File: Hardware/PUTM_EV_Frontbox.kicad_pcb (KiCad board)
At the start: 4 copper layers, 97 x 73 mm, 188 parts, among them IC1 TPS54202HDDCR, J1 XIAO ESP32S3 Sense, J2 Conn_02x16_Counter_Clockwise, J3 FTSH-107-01-L-D-K, Q1 SI2347DS-T1-GE3, U1 TLV743P, U10 MCP6N11-001E/SN, U11 MCP6002-xSN, U12 TLP291-4, U13 TLP291-4, U14 FODM217B, U2 TLV743P, U3 TLV743P, U4 TLV743P, U5 LM4040C33FTA, U6 STM32G484RETx, U7 ADM3057ExRW, U8 ADM3057ExRW, U9 MCP6N11-001E/SN, Y1 ATX-11-F-32.000MHZ-F05-T

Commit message: BOM update
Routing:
- net Net-(R20-Pad1): track 15.1 -> 17.8 mm, vias 0 -> 2
- net /APPS_POT_1: track 40.6 -> 43.0 mm
- net Net-(R27-Pad1): track 14.9 -> 17.2 mm, vias 0 -> 2
- net /DAC2_REF: track 51.9 -> 53.3 mm
- net /APPS_POT_2: track 53.2 -> 54.6 mm
- net +5V: track 150.6 -> 151.3 mm

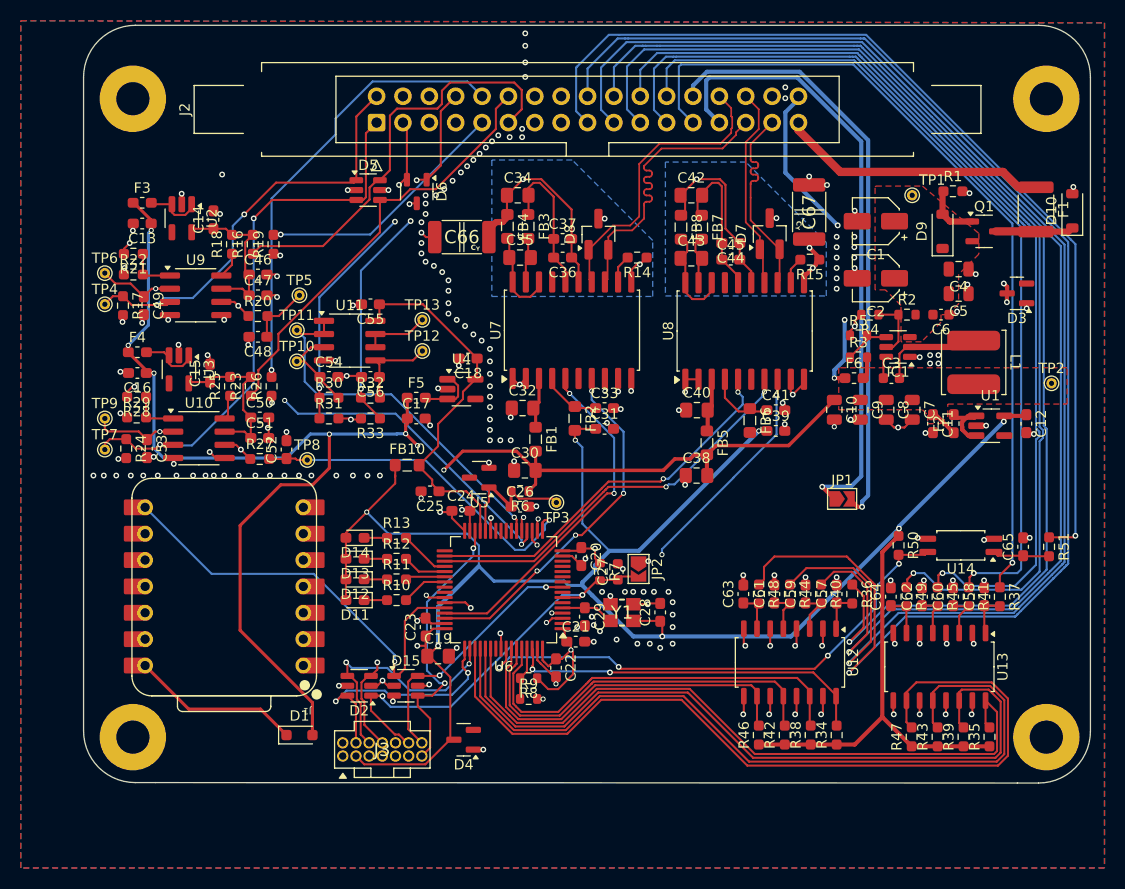
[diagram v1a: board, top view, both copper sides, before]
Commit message: Silkscreen changes
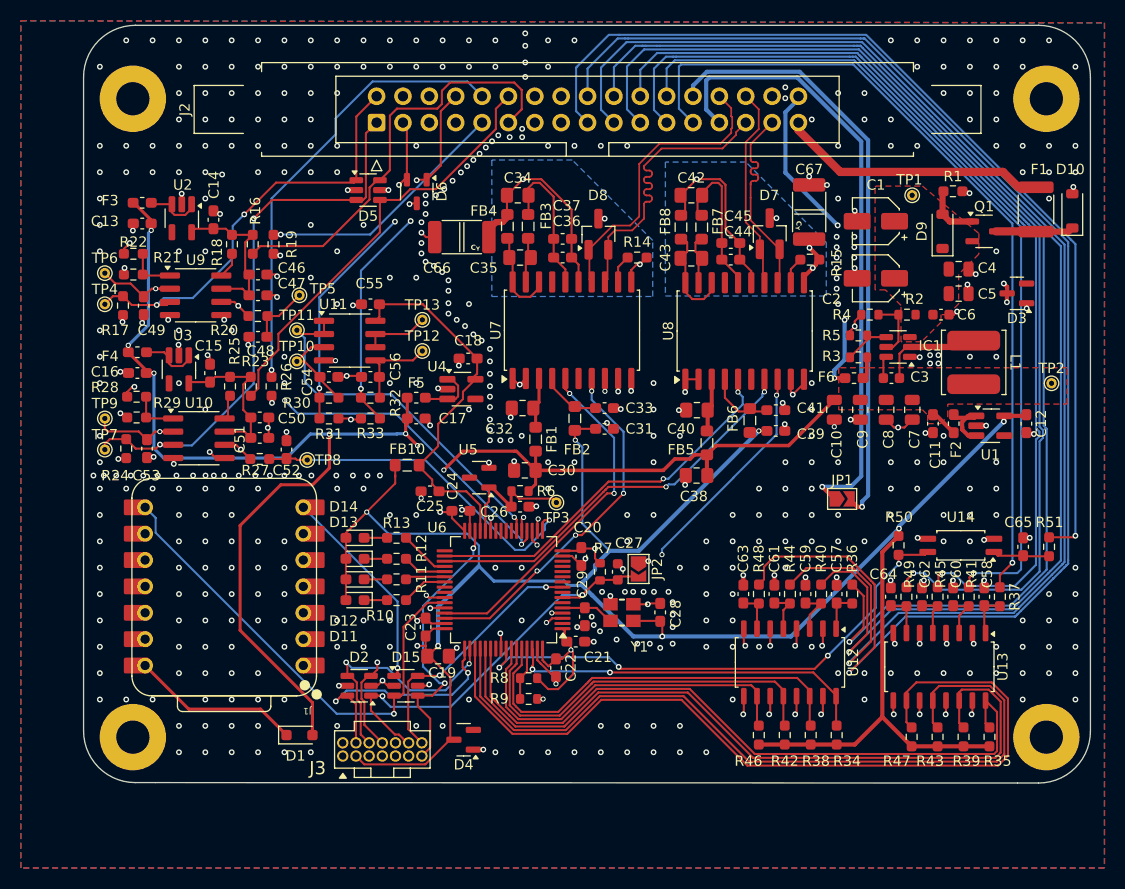
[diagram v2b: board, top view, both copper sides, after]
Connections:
- J1 pad 7: /Connector/UART_TX -> /Connector/UART_RX
- J1 pad 8: /Connector/UART_RX -> /Connector/UART_TX
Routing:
- net /Connector/UART_RX: track 42.3 -> 29.1 mm, vias 1 -> 2
- net /Connector/UART_TX: track 38.9 -> 47.1 mm, vias 2 -> 1
- net GND: vias 211 -> 525

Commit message: Added Tensionmeters initial version
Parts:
- added C68: 1u, Capacitor_SMD:C_0603_1608Metric, B.Cu at (136.5, 120.0)
- added C69: 1n, Capacitor_SMD:C_0603_1608Metric, B.Cu at (136.5, 122.5)
- added C70: 100n, Capacitor_SMD:C_0603_1608Metric, B.Cu at (137.5, 128.0)
- added C71: 1u, Capacitor_SMD:C_0603_1608Metric, B.Cu at (126.5, 132.0)
- added C72: 100n, Capacitor_SMD:C_0603_1608Metric, F.Cu at (142.0, 122.0)
- added C73: 330n, Capacitor_SMD:C_0603_1608Metric, F.Cu at (142.5, 126.5)
- added C74: 100n, Capacitor_SMD:C_0603_1608Metric, B.Cu at (130.0, 128.0)
- added C75: 1u, Capacitor_SMD:C_0603_1608Metric, B.Cu at (137.5, 132.0)
- added C76: 100n, Capacitor_SMD:C_0603_1608Metric_Pad1.08x0.95mm_HandSolder, B.Cu at (122.5, 134.0)
- added G***: LOGO, Samacsys:PUTM_Logo_8mm, B.Cu at (128.9, 142.1)
- added IC2: MCP1501T-18E_CHY, Samacsys:SOT95P270X145-6N, B.Cu at (133.0, 121.5)
- added R111: 100K, Resistor_SMD:R_0603_1608Metric, B.Cu at (123.0, 130.0)
- added R112: 100K, Resistor_SMD:R_0603_1608Metric, B.Cu at (134.0, 130.0)
- added R75: 1k, Resistor_SMD:R_0603_1608Metric, B.Cu at (126.5, 128.0)
- added R76: 330, Resistor_SMD:R_0603_1608Metric, B.Cu at (126.5, 130.0)
- added R77: 1k, Resistor_SMD:R_0603_1608Metric, B.Cu at (134.0, 128.0)
- added R78: 330, Resistor_SMD:R_0603_1608Metric, B.Cu at (137.5, 130.0)
- added TP47: BR_N, TestPoint:TestPoint_Pad_D1.0mm, B.Cu at (123.0, 127.5)
- added TP48: BR_N, TestPoint:TestPoint_Pad_D1.0mm, B.Cu at (131.5, 130.5)
- added TP49: BR_N, TestPoint:TestPoint_Pad_D1.0mm, B.Cu at (130.0, 122.5)
- added TP50: BR_N, TestPoint:TestPoint_Pad_D1.0mm, B.Cu at (127.5, 122.5)
- added TP51: BR_N, TestPoint:TestPoint_Pad_D1.0mm, B.Cu at (123.5, 132.0)
- added TP52: BR_N, TestPoint:TestPoint_Pad_D1.0mm, B.Cu at (134.5, 132.0)
- added TP53: BR_N, TestPoint:TestPoint_Pad_D1.0mm, B.Cu at (129.0, 131.5)
- added TP54: BR_N, TestPoint:TestPoint_Pad_D1.0mm, B.Cu at (133.5, 136.1)
- added U15: L7812, Package_TO_SOT_SMD:TO-263-2, F.Cu at (130.4, 125.7)
- added U16: MCP6002-xSN, Package_SO:SOIC-8_3.9x4.9mm_P1.27mm, B.Cu at (128.5, 135.5)
- added U24: AD8226BRMZ-R7, Snapeda:AD8226BRMZ-R7_SOP65P490X110-8N, B.Cu at (127.5, 125.5)
- added U25: AD8226BRMZ-R7, Snapeda:AD8226BRMZ-R7_SOP65P490X110-8N, B.Cu at (135.0, 125.5)
- moved JP1 9.50 mm to (145.0, 124.5)
- moved R50 0.54 mm to (141.5, 129.7)
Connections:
- J2 pad 15: unconnected-(J2-Pin_15-Pad15) -> +12V
- J2 pad 4: unconnected-(J2-Pin_4-Pad4) -> /Connector/Tens_Out1+
- J2 pad 5: unconnected-(J2-Pin_5-Pad5) -> /Connector/Tens_Out1-
- J2 pad 6: unconnected-(J2-Pin_6-Pad6) -> /Connector/Tens_Out2+
- J2 pad 7: unconnected-(J2-Pin_7-Pad7) -> /Connector/Tens_Out2-
- U6 pad 12: unconnected-(U6-PA0-Pad12) -> /MCU/Tens1
- U6 pad 13: unconnected-(U6-PA1-Pad13) -> /MCU/Tens2
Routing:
- net +12V: track 0.00 -> 128.0 mm, vias 0 -> 2
- net /Connector/Tens_Out2+: track 0.00 -> 95.0 mm, vias 0 -> 1
- net /Connector/Tens_Out2-: track 0.00 -> 80.8 mm, vias 0 -> 1
- net /Connector/Tens_Out1+: track 0.00 -> 77.6 mm, vias 0 -> 1
- net /Connector/Tens_Out1-: track 0.00 -> 69.4 mm, vias 0 -> 1
- net /MCU/Tens1: track 0.00 -> 40.9 mm, vias 0 -> 2
- net +3.3V: track 281.3 -> 310.2 mm
- net /MCU/Tens2: track 0.00 -> 27.7 mm, vias 0 -> 2
- net +24V: track 0.00 -> 24.9 mm, vias 0 -> 2
- net Net-(U16B-+): track 0.00 -> 19.6 mm
- net Net-(U16A-+): track 0.00 -> 18.0 mm
- net /Tensionmeter/1,8V: track 0.00 -> 17.4 mm
- net Net-(U25-VOUT): track 0.00 -> 6.64 mm
- net Net-(U24-VOUT): track 0.00 -> 5.70 mm
- net GND: track 121.8 -> 127.2 mm, vias 525 -> 218
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
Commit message: Fused 12V
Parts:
- added F7: 300mA, Fuse:Fuse_0603_1608Metric_Pad1.05x0.95mm_HandSolder, F.Cu at (144.0, 121.4)
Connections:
- C72 pad 1: +12V -> Net-(U15-OUT)
- U15 pad 3: +12V -> Net-(U15-OUT)
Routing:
- net Net-(U15-OUT): track 0.00 -> 6.54 mm
- net GND: track 127.2 -> 130.4 mm, vias 218 -> 222
- net +12V: track 128.0 -> 126.6 mm

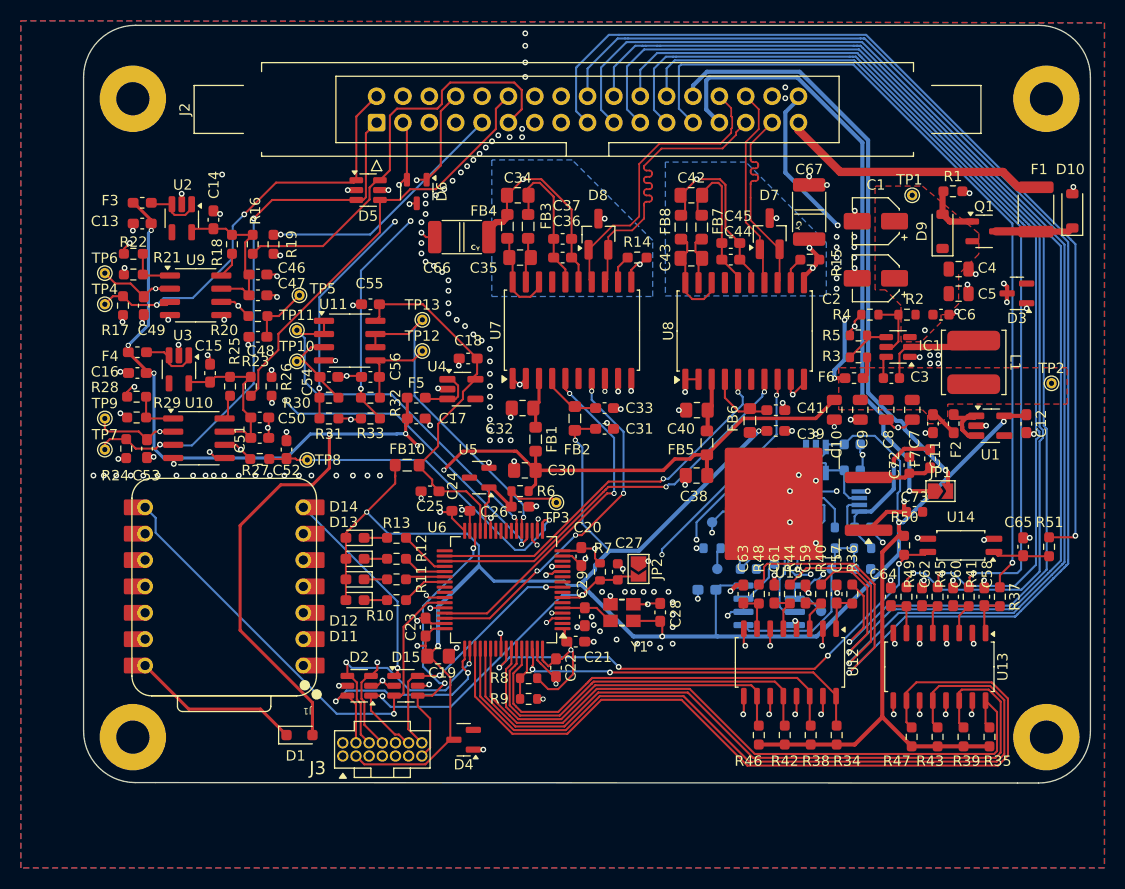
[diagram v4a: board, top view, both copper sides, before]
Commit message: Added tensionmeter section, updated APPS resistors for transfer function
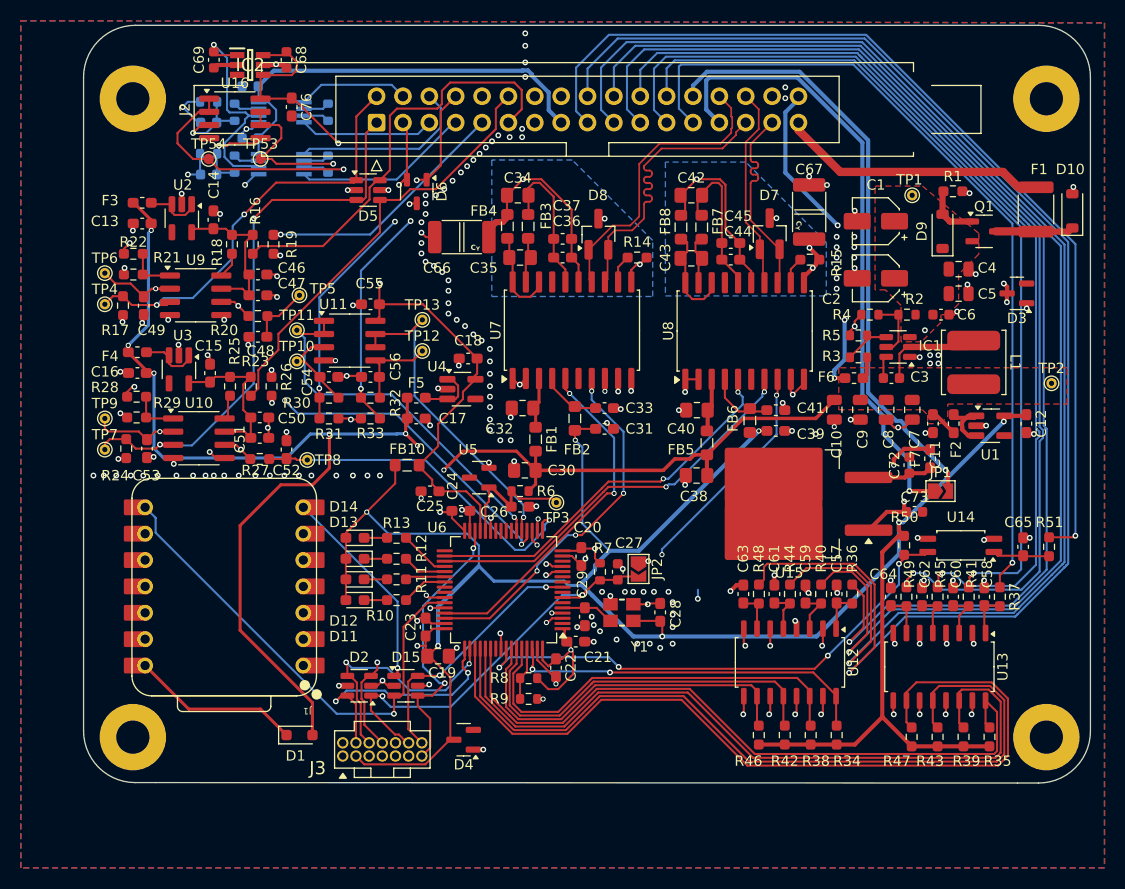
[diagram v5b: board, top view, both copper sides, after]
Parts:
- removed TP47, TP48, TP49, TP50, TP51, TP52: BR_N, TestPoint:TestPoint_Pad_D1.0mm
- C68, C69, C76, IC2, TP53, TP54, U16: moved to F.Cu
- moved C75 73.6 mm to (74.5, 94.0), turned to 180 degrees
- moved TP54 73.3 mm to (74.5, 92.5), turned to 0 degrees
- moved C69 73.1 mm to (75.0, 83.0), turned to 90 degrees
- moved C70 72.7 mm to (78.5, 85.5), turned to 180 degrees
- moved R78 70.9 mm to (77.0, 93.0), turned to -90 degrees
- moved R112 70.6 mm to (74.5, 92.0)
- moved U16 69.6 mm to (77.0, 88.6), turned to 0 degrees
- moved C71 67.5 mm to (74.5, 89.0), turned to 180 degrees
- moved IC2 66.5 mm to (78.5, 83.5), turned to 0 degrees
- moved C68 65.9 mm to (82.0, 83.0), turned to -90 degrees
- moved R76 64.9 mm to (77.0, 88.0), turned to -90 degrees
- moved R111 64.8 mm to (74.5, 87.0)
- moved C74 63.7 mm to (78.5, 90.5), turned to 180 degrees
- moved TP53 63.0 mm to (79.5, 92.5), turned to 0 degrees
- moved U25 62.6 mm to (81.5, 93.0), turned to 180 degrees
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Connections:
- C68 pad 1: +3.3V -> +3.3VA
- C76 pad 1: +3.3V -> +3.3VA
- IC2 pad 4: +3.3V -> +3.3VA
- IC2 pad 6: +3.3V -> +3.3VA
- J2 pad 4: /Connector/Tens_Out1+ -> /Connector/Tens_Out1-
- J2 pad 5: /Connector/Tens_Out1- -> /Connector/Tens_Out1+
- J2 pad 6: /Connector/Tens_Out2+ -> /Connector/Tens_Out2-
- J2 pad 7: /Connector/Tens_Out2- -> /Connector/Tens_Out2+
- U16 pad 8: +3.3V -> +3.3VA
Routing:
- net /Connector/Tens_Out2+: track 95.0 -> 17.1 mm, vias 1 -> 0
- net /Connector/Tens_Out1+: track 77.6 -> 13.0 mm, vias 1 -> 0
- net /Connector/Tens_Out2-: track 80.8 -> 17.7 mm, vias 1 -> 0
- net /Connector/Tens_Out1-: track 69.4 -> 10.7 mm, vias 1 -> 0
- net /MCU/Tens2: track 27.7 -> 71.0 mm
- net /MCU/Tens1: track 40.9 -> 79.9 mm
- net +3.3VA: track 36.8 -> 74.0 mm, vias 0 -> 2
- net +3.3V: track 310.2 -> 284.7 mm
- net Net-(U16B-+): track 19.6 -> 8.97 mm, vias 0 -> 1
- net Net-(U16A-+): track 18.0 -> 8.38 mm, vias 0 -> 1
- net GND: track 130.4 -> 137.6 mm, vias 222 -> 216
- net +12V: track 126.6 -> 133.8 mm, vias 2 -> 1
- net /Tensionmeter/1,8V: track 17.4 -> 21.8 mm, vias 0 -> 1
- net Net-(U25-VOUT): track 6.64 -> 2.52 mm
- net Net-(U24-VOUT): track 5.70 -> 2.52 mm
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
